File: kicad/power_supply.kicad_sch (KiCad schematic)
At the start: 19 parts, among them T1 reuse / AnTek AS-0524, U1 LM317T

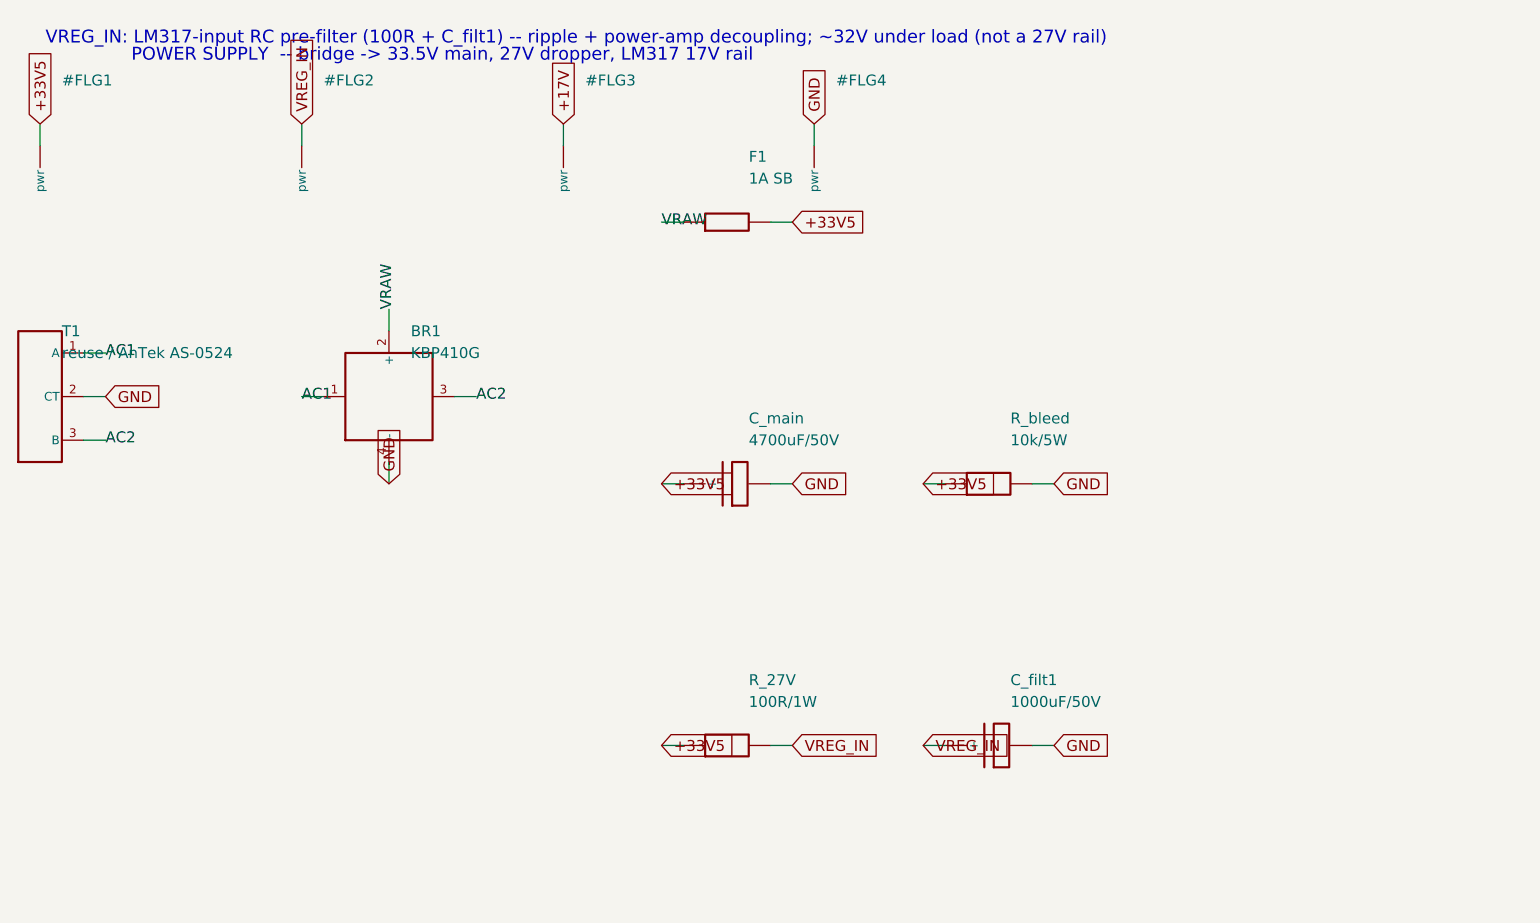
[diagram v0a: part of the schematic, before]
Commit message: Generate BOM from schematic (authoritative); complete missing schematic parts
The BOM had drifted badly from the schematic (~20 parts in the schematic missing
from the BOM, ~20 stale/renamed rows in the BOM). Root-caused two ways:

1. Completed the SCHEMATIC -- added parts that were in Part 2 / the BOM but never
   actually placed: rectifier snubbers C101-C104, 2nd pre-filter C_filt2, and the
   tremolo SPEED/DEPTH pots (POT_SPD as a rheostat in the Wien series arm to vary
   frequency; POT_DPT scaling the LFO into the VTL1 LED for depth). 117 comps, ERC 0.

2. Made the BOM GENERATED from the schematic: kicad/gen/gen_bom.py emits bom/bom.csv
   per-reference 1:1 with the netlist (verified: every schematic ref present),
   merged with curated part numbers/notes and an explicit off-board/mechanical
   section (sockets, heatsink, mica, standoffs, fuses, mains fuse). Also writes
   bom/bom-grouped.csv (consolidated by value+footprint for ordering). bom/README
   updated to say it's generated; do not hand-edit.

Verified: sch erc 0, demo DRC 0, run_all.sh exit 0, BOM 8-col clean, every
schematic ref covered. Full board now 113 footprints; density 53%/90% (190x115 /
155x90) -- reinforces the chassis-fit finding.

https://claude.ai/code/session_01PkrfUi9tvZfLvudJ7h23qD
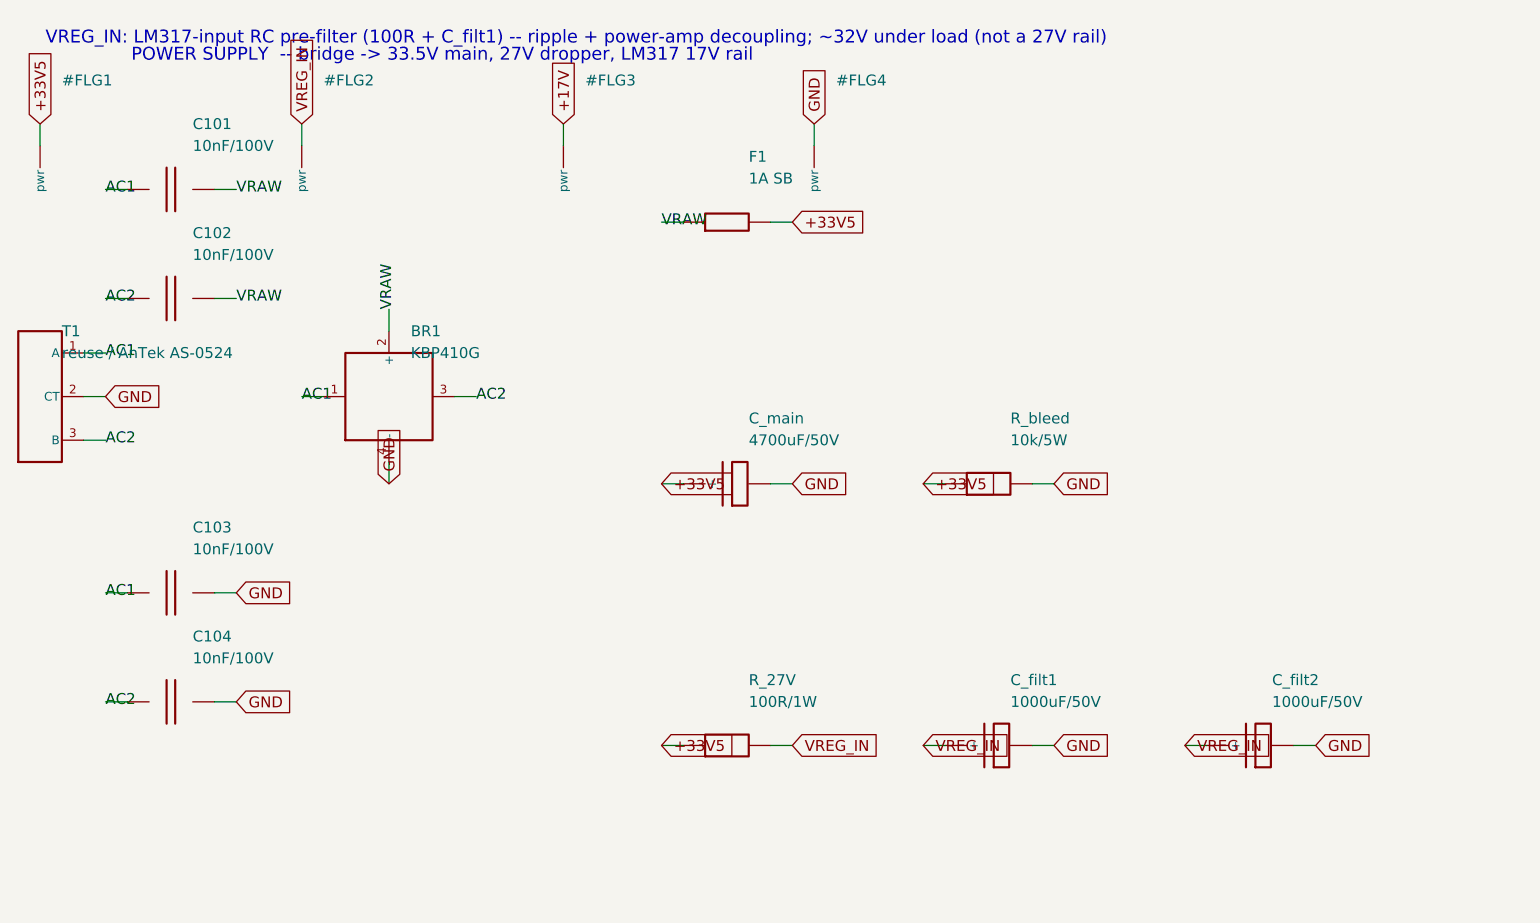
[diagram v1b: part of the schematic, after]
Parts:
- added C101, C102, C103, C104: 10nF/100V, Capacitor_THT:C_Disc_D7.5mm_W2.5mm_P5.00mm, symbol cr_primitives:C
- added C_filt2: 1000uF/50V, Capacitor_THT:CP_Radial_D8.0mm_P3.50mm, symbol cr_primitives:CP
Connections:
- net AC1: now also C101.1, C103.1
- net AC2: now also C102.1, C104.1
- net GND: now also C103.2, C104.2, C_filt2.2
- net VRAW: now also C101.2, C102.2
- net VREG_IN: now also C_filt2.1 (+)
